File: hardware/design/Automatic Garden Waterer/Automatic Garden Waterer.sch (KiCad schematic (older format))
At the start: 27 parts

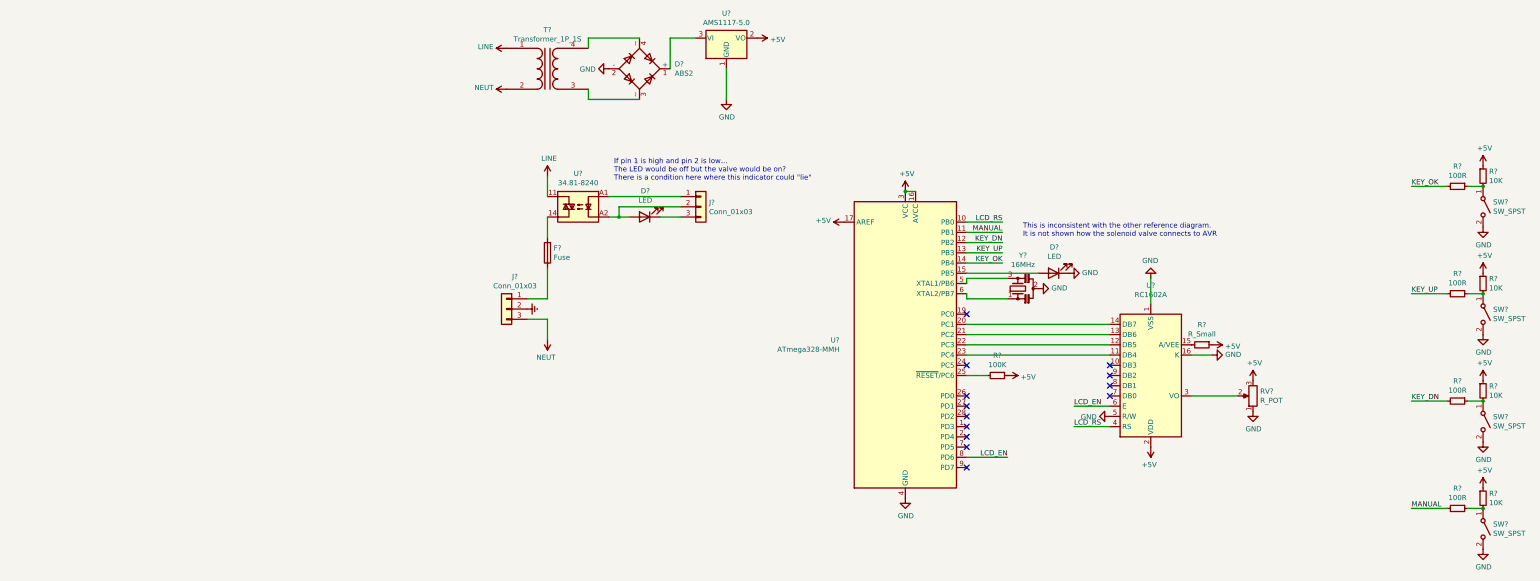
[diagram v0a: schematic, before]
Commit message: modified valve control circuit for UX/UI clarity
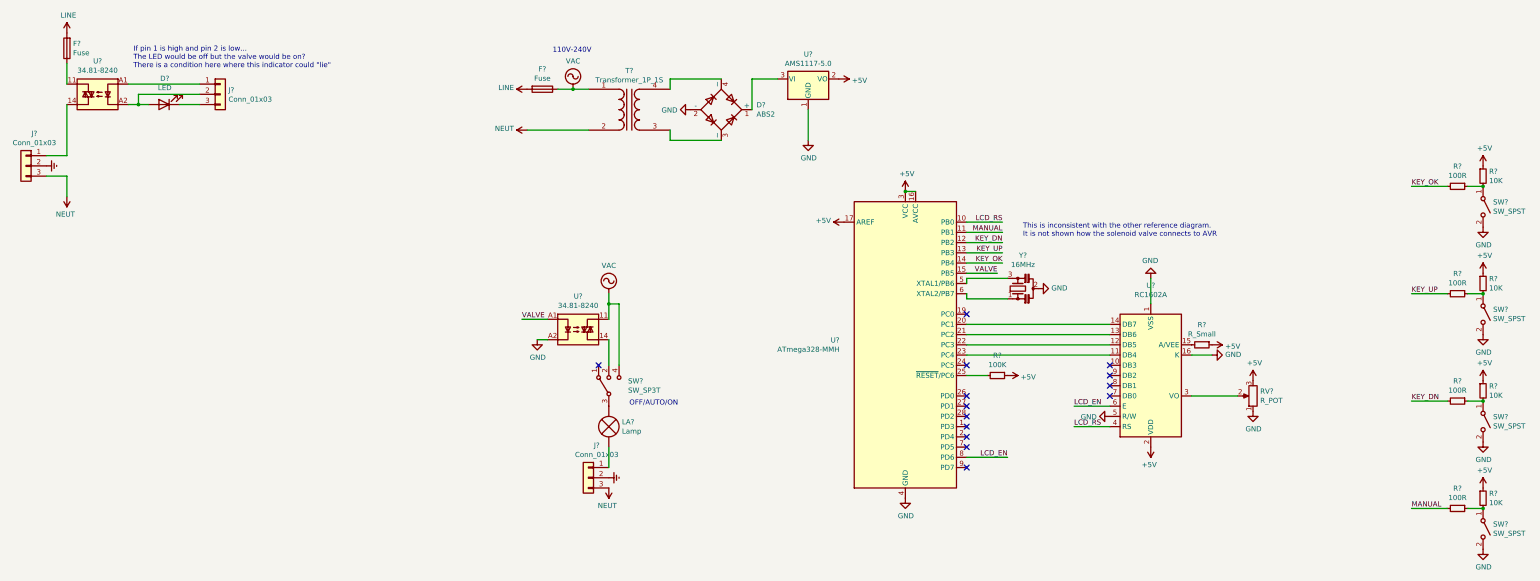
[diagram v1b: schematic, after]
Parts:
- removed D?: LED, symbol Device:LED
- added F?: Fuse, symbol Device:Fuse
- added J?: Conn_01x03, symbol Connector_Generic:Conn_01x03
- added LA?: Lamp, symbol Device:Lamp
- added SW?: SW_SP3T, symbol Switch:SW_SP3T
- added U?: 34.81-8240, OptoDevice:Finder_34.81, symbol Relay_SolidState:34.81-8240
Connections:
- net Earth: now also J?.2 (Pin_2)
- net GND: now also U?.A2
- net LINE: now also F?.2, F?.2; no longer T?.1 (AA), U?.11
- net NEUT: now also J?.3 (Pin_3)
- net at J?.1 (Pin_1): now also U?.14; no longer F?.1
- net VALVE: now reaches U?.15 (PB5)
- net VALVE: now also U?.A1
- new net: F?.1, U?.11
- new net: SW?.2, U?.14
- new net: LA?.2 (+), SW?.3
- new net: J?.1 (Pin_1), LA?.1 (-)
- new net VAC: F?.1, SW?.4, T?.1 (AA), U?.11
- no-connect marks 13 -> 14
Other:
- note added: "110V-240V"
- note added: "OFF/AUTO/ON"
- moved on the sheet: D?, F?, J?, T?, U?
